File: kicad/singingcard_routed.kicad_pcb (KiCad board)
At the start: 2 copper layers, 85 x 55 mm, 16 parts, among them J1 Speaker 8ohm, J2 Pull-Tab, SW1 Button, U1 ISD3900FYI, U2 W25Q16JVSSIQ

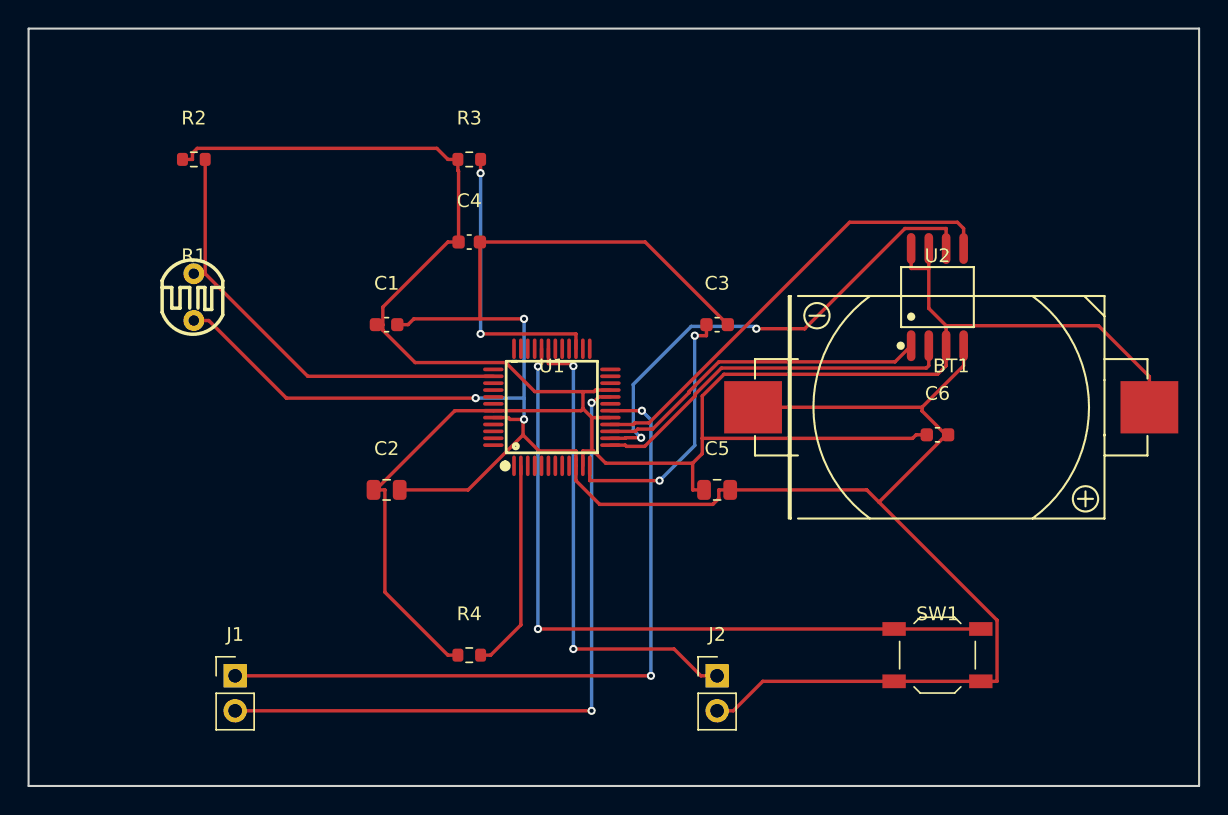
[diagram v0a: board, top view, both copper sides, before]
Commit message: Add SMD speaker, fix component placement, clean up renders
- Replace J1 connector with LS1 SMD speaker (KLJ-01304T-08R07W, LCSC C18186315)
- Move U2 and C6 outside battery holder area to prevent overlap
- Move battery holder to meet 0.5mm edge clearance requirement
- Re-route PCB with FreeRouting (181 tracks, 21 vias)
- DRC passes with 0 errors, 0 unconnected items
- Change schematic page size from A3 to A4
- Clean up old render images, keep only current versions
- Update fabrication files (JLCPCB-ready zip)

🤖 Generated with [Claude Code](https://claude.com/claude-code)

Co-Authored-By: Claude <noreply@anthropic.com>
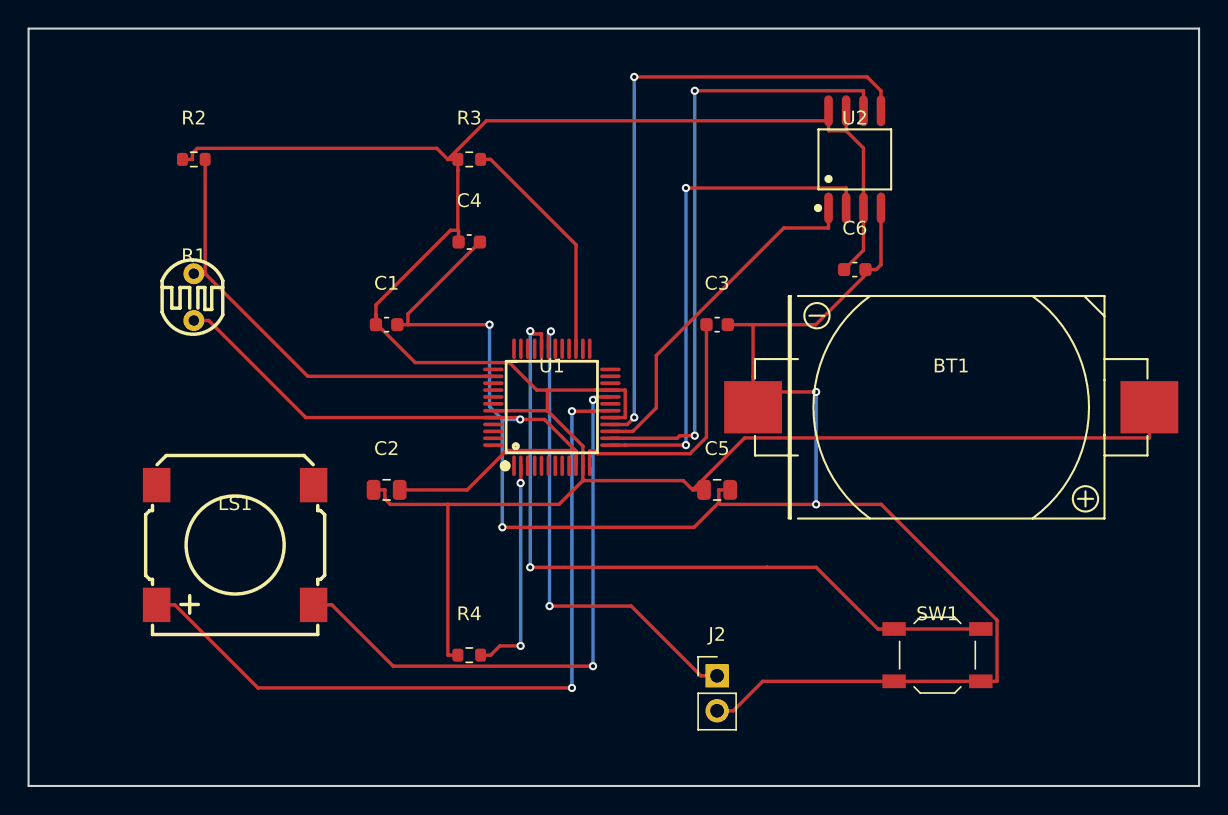
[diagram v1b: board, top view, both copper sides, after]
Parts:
- removed J1: Speaker 8ohm, Connector_PinHeader_2.54mm:PinHeader_1x02_P2.54mm_Vertical
- added LS1: KLJ-01304T-08R07W, speaker:BUZ-SMD_4P-L13.0-W13.0-P11.4-BL, F.Cu at (115.0, 137.5)
- moved C6 13.4 mm to (160.0, 117.5)
- moved U2 11.7 mm to (160.0, 109.5)
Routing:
- net (no net): track 0.00 -> 98.4 mm, vias 0 -> 4
- net N$1: track 52.0 -> 0.00 mm, vias 2 -> 0
- net N$2: track 49.8 -> 0.00 mm, vias 2 -> 0
- net +3V: track 176.4 -> 190.6 mm
- net SPI_MOSI: track 33.4 -> 46.5 mm, vias 0 -> 2
- net SPI_MISO: track 27.1 -> 37.2 mm, vias 0 -> 2
- net SPI_SCK: track 35.4 -> 45.0 mm
- net RESET: track 20.7 -> 17.0 mm, vias 2 -> 0
- net GND: track 179.0 -> 181.8 mm, vias 3 -> 5
- net SPI_CS: track 24.5 -> 25.6 mm
- net VREG: track 19.4 -> 18.3 mm, vias 2 -> 0
- net GPIO1_BTN: track 52.7 -> 53.7 mm
- net CSB: track 15.4 -> 16.3 mm, vias 0 -> 2
- net GPIO2_TAB: track 34.8 -> 35.6 mm
